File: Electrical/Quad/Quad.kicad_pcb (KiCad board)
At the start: 2 copper layers, 140 x 70 mm, 133 parts, among them J101 01x04, J102 01x04, J103 01x03, J104 01x03, J201 01x03, J202 01x04, J203 01x03, J204 01x04, J205 01x03, J206 USB_OTG, J207 01x04, J208 01x02, J209 01x04, J210 01x02, J211 01x02, J212 4PostTerm, J213 2PostTerm, J214 2PostTerm, J215 2PostTerm, J216 2PostTerm, J217 2PostTerm, J218 01x02, J219 01x02, Q201 FDC6420C, Q202 FDG1024NZ, Q301 FDC6420C, Q401 FDC6420C, Q501 FDC6420C, Q601 FDC6420C, U201 TPD4S012, U202 ACS723LLCTR-05AB-T, U203 ACS723LLCTR-05AB-T, U204 24LC256, U205 LM2576HVS-ADJ, U206 LM2576HVS-ADJ

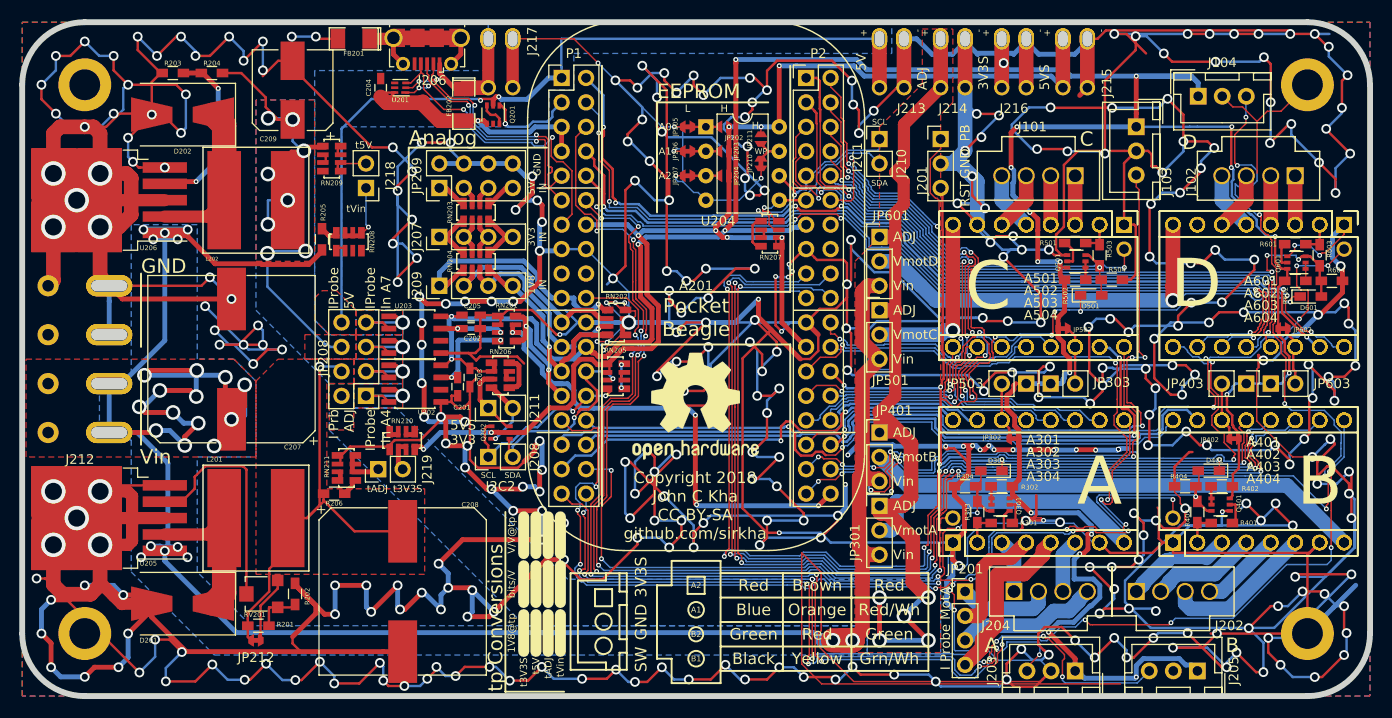
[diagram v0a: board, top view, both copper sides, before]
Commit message: Rearranged the power outputs to support TE Connectivity AMP connectors.
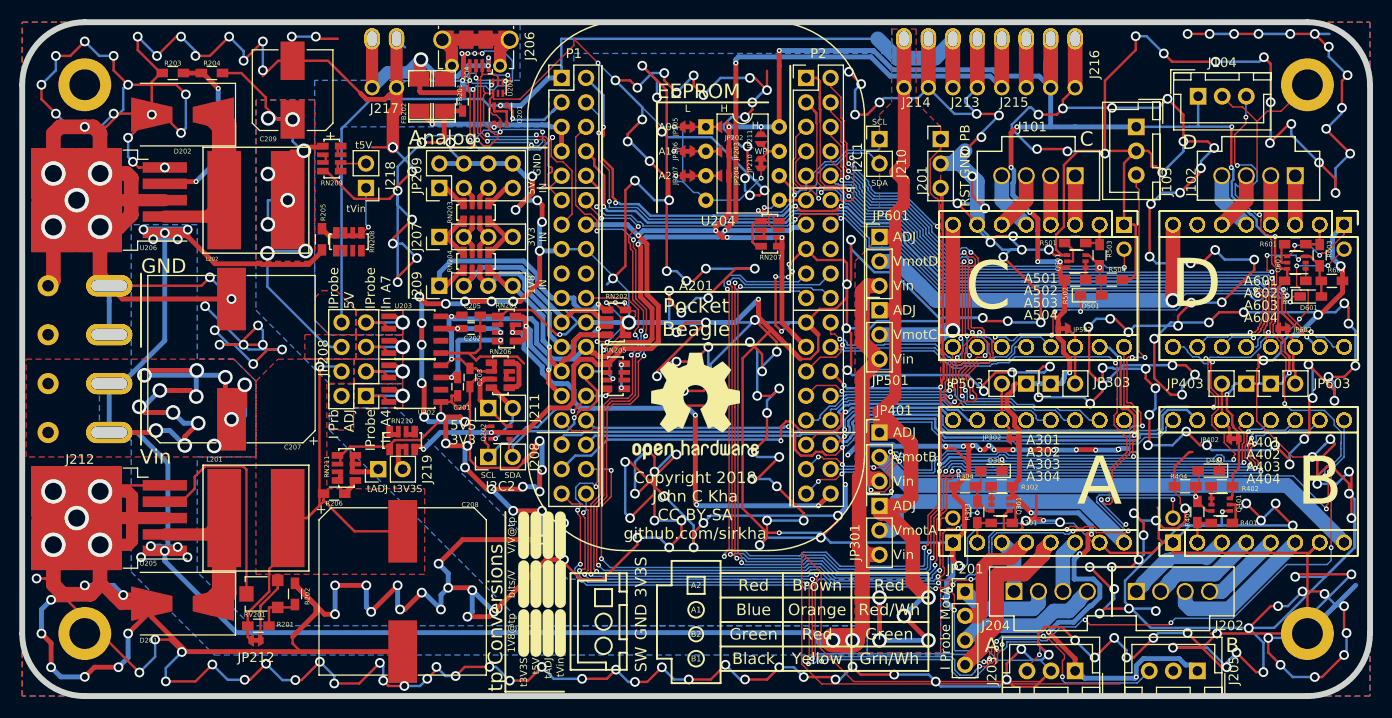
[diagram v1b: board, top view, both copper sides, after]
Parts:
- moved J217 12.1 mm to (67.6, 69.3)
- moved FB201 11.1 mm to (73.8, 72.6), turned to 90 degrees
- moved U201 10.2 mm to (79.4, 71.8), turned to 270 degrees
- moved C204 8.63 mm to (75.7, 73.3), turned to 270 degrees
- moved J213 7.62 mm to (127.9, 69.3)
- moved J215 6.35 mm to (133.0, 69.3)
- moved J206 5.08 mm to (77.1, 67.2)
- moved J216 5.08 mm to (138.1, 69.3)
- moved FB202 4.68 mm to (71.3, 72.6), turned to 90 degrees
- moved J214 3.81 mm to (122.9, 69.3)
- moved Q201 0.76 mm to (79.7, 74.6)
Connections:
- C204 pad 1: /Common/usb1_vbus -> /Common/usb1_5V
- FB201 pad 1: Net-(FB201-Pad1) -> GND
- FB201 pad 2: GND -> Net-(FB201-Pad2)
- FB202 pad 1: /Common/usb1_5V -> /Common/usb1_vbus
- FB202 pad 2: /Common/usb1_vbus -> /Common/usb1_5V
- J206 pad 6: Net-(FB201-Pad1) -> Net-(FB201-Pad2)
- U201 pad 6: /Common/usb1_vbus -> /Common/usb1_5V
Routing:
- net GND: track 2509.9 -> 2550.2 mm, vias 393 -> 404
- net 3V3S: track 353.1 -> 328.8 mm, vias 27 -> 25
- net Net-(FB201-Pad1): track 22.1 -> 0.00 mm
- net /Common/usb1_5V: track 11.8 -> 33.4 mm, vias 0 -> 4
- net Net-(FB201-Pad2): track 0.00 -> 15.0 mm
- net +5V: track 89.0 -> 97.5 mm, vias 2 -> 1
- net /Common/usb1_vbus: track 27.3 -> 18.9 mm, vias 1 -> 2
- net Vadj: track 98.5 -> 91.7 mm
- net 5VS: track 126.8 -> 120.7 mm
- net /Common/usb1_d-: track 29.0 -> 23.8 mm, vias 4 -> 2
- net (no net): track 0.00 -> 4.88 mm, vias 0 -> 2
- net /Common/usb1_d+: track 28.0 -> 25.3 mm
- net /Common/usb1_drvvbus: track 9.68 -> 10.2 mm, vias 2 -> 1
- net /Common/usb1_id: track 32.6 -> 32.7 mm, vias 2 -> 5
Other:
- outline, holes or cut-outs redrawn

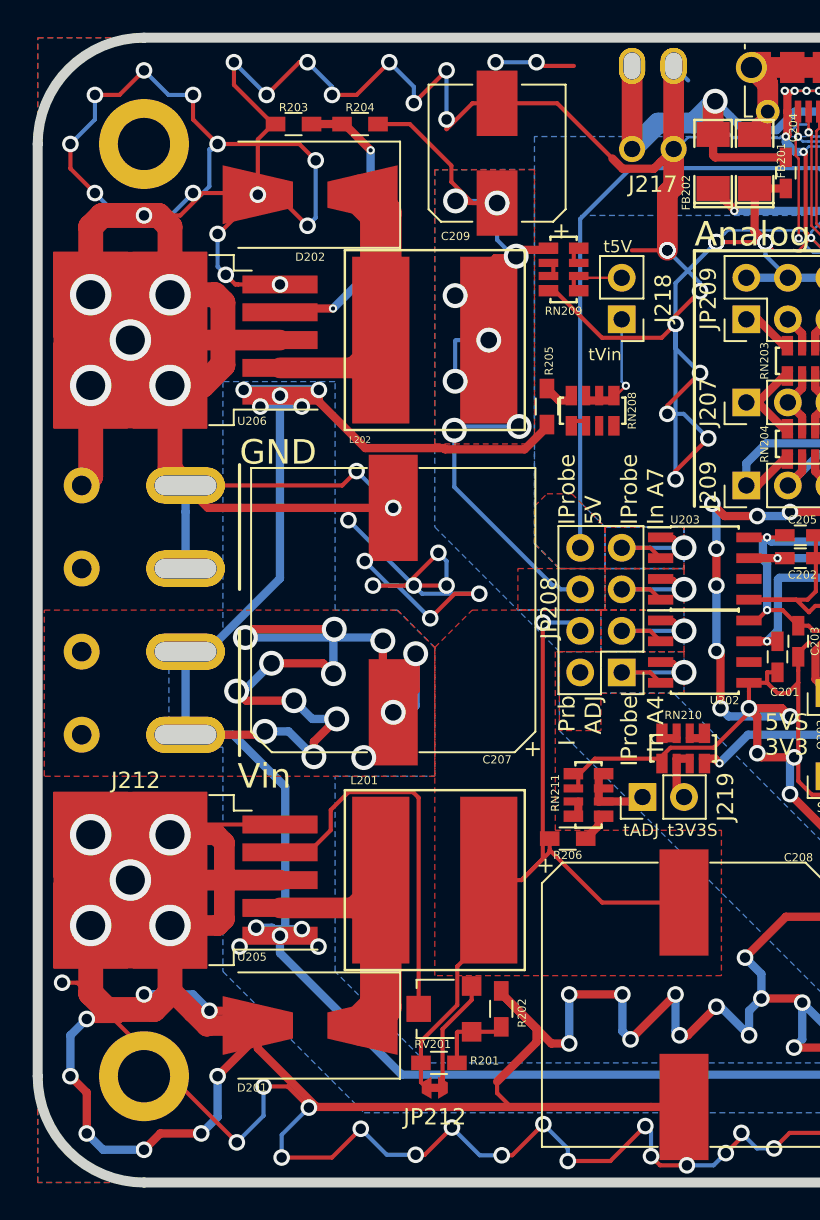
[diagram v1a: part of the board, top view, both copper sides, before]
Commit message: Modified main power input footprint to support other connectors
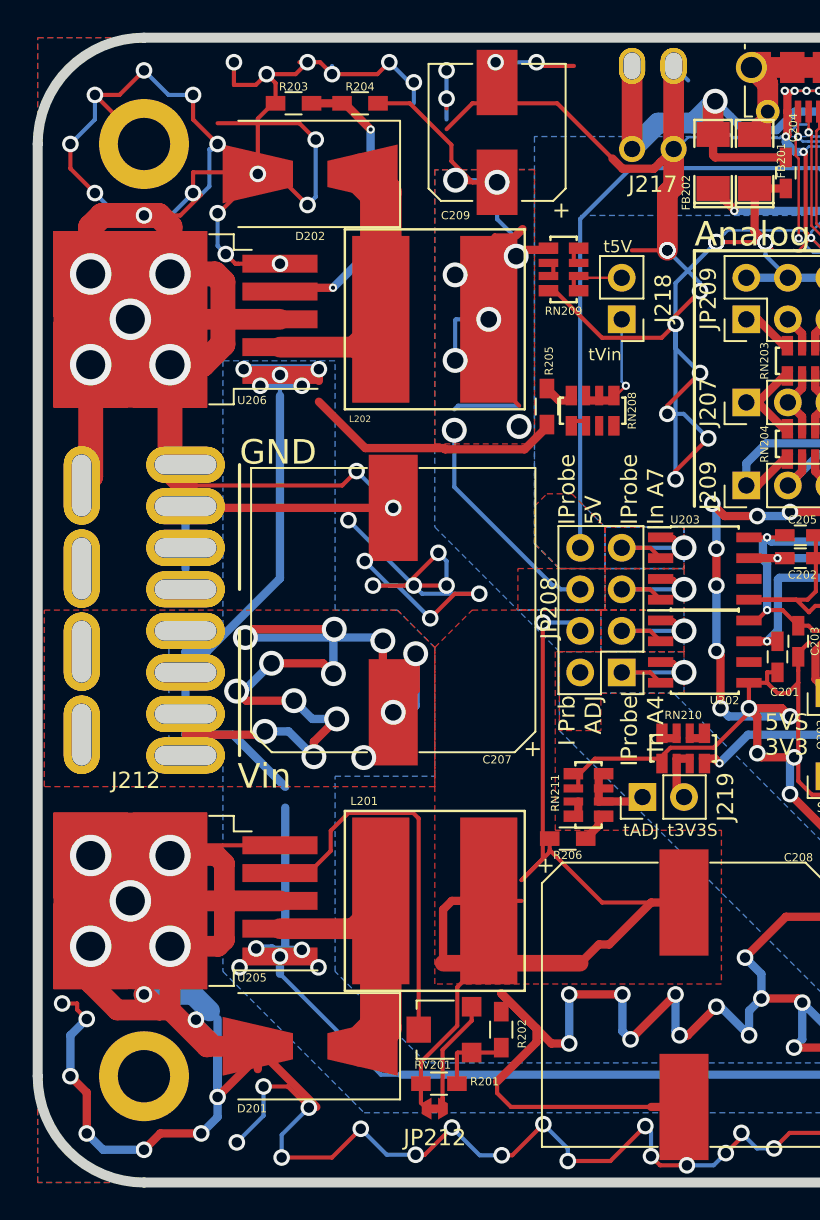
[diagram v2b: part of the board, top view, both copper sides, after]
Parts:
- moved C209 1.27 mm to (58.1, 70.8)
- moved D201 1.27 mm to (46.7, 126.7)
- moved D202 1.27 mm to (46.7, 73.3)
- moved L201 1.27 mm to (54.3, 117.8)
- moved L202 1.27 mm to (54.3, 82.2)
- moved R202 1.27 mm to (58.3, 125.7)
- moved R203 1.27 mm to (45.6, 69.0)
- moved R204 1.27 mm to (49.7, 69.0)
- moved RV201 1.27 mm to (54.9, 125.7)
- moved U205 1.27 mm to (39.0, 117.8)
- moved U206 1.27 mm to (39.0, 82.2)
- moved JP212 1.27 mm to (54.3, 130.5)
- moved R201 1.27 mm to (54.5, 129.0)
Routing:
- net GND: track 2550.2 -> 2514.6 mm
- net /Common/IP_vadj: track 48.1 -> 70.7 mm
- net /Common/IP_5V: track 57.0 -> 53.0 mm, vias 8 -> 7
- net (no net): track 4.88 -> 7.65 mm, vias 2 -> 3
- net Vin: track 273.4 -> 274.0 mm
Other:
- outline, holes or cut-outs redrawn

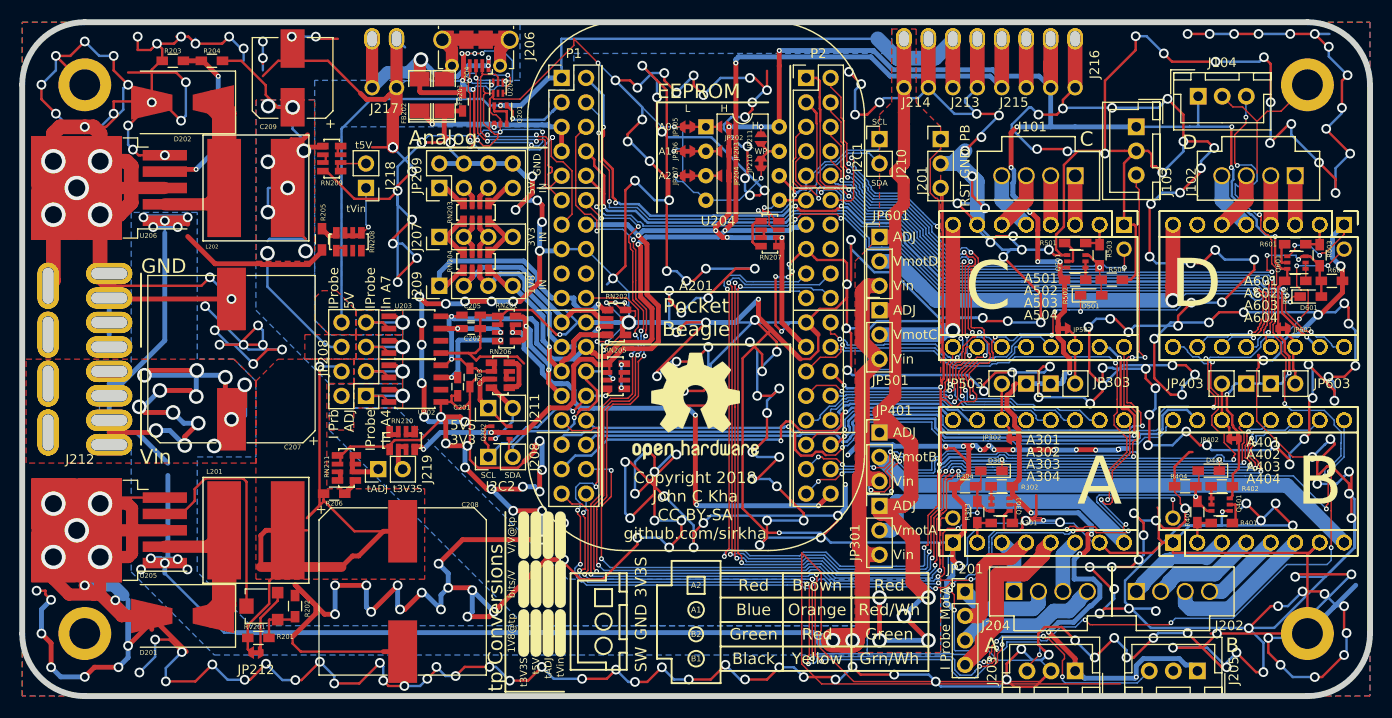
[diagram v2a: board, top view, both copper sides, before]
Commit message: Rearranged EEPROM to add an MSOP option and make the address/WP pins more accessible
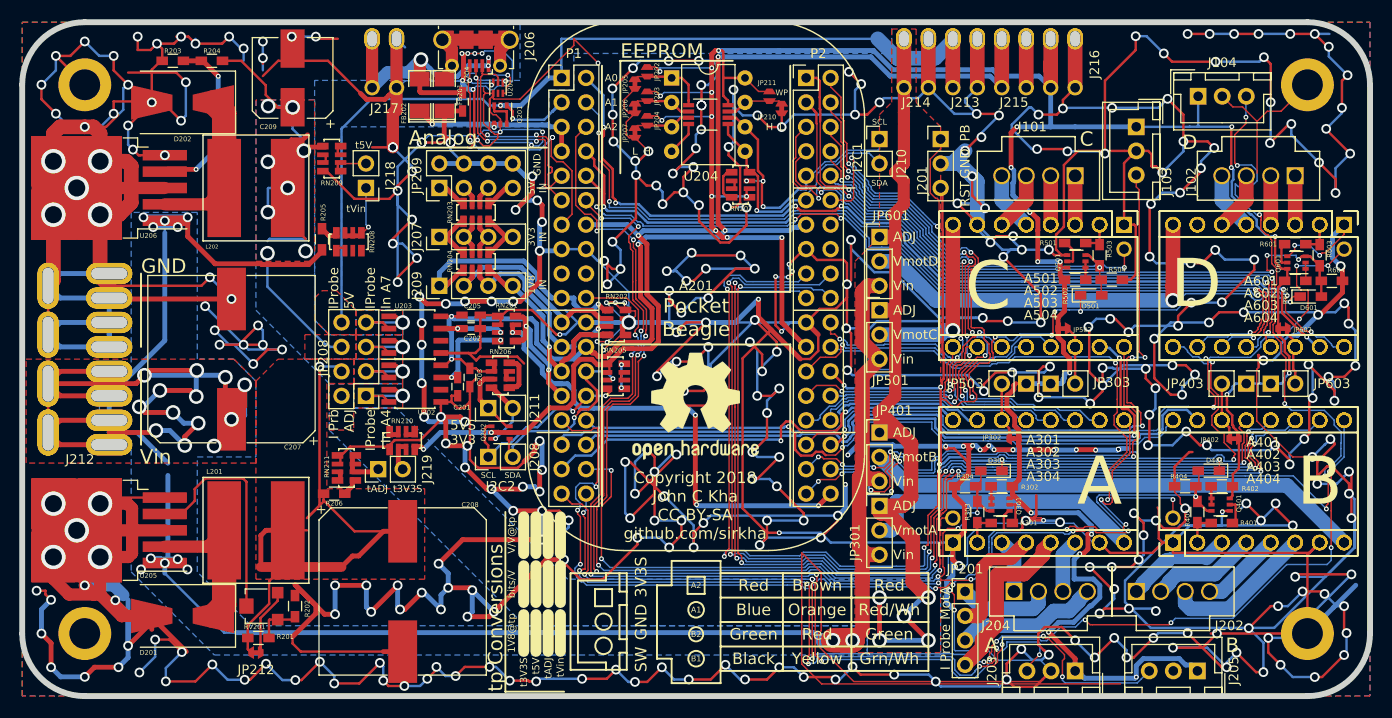
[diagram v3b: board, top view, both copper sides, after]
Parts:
- U204: footprint Housings_DIP:DIP-8_W7.62mm -> footprints:Dip-MSOP-8
- moved JP202 9.83 mm to (94.9, 70.2), turned to 270 degrees
- moved JP203 9.83 mm to (94.9, 72.7), turned to 270 degrees
- moved JP204 9.83 mm to (94.9, 75.2), turned to 270 degrees
- moved JP205 7.04 mm to (93.7, 71.4), turned to 90 degrees
- moved JP207 7.04 mm to (93.7, 76.5), turned to 90 degrees
- moved JP206 7.04 mm to (93.7, 74.0), turned to 90 degrees
- moved U204 6.20 mm to (97.5, 70.8)
- moved JP210 6.11 mm to (108.9, 74.0)
- moved RN207 5.92 mm to (104.6, 81.9)
- moved JP211 4.53 mm to (107.6, 72.7)
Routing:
- net Vin: track 274.0 -> 322.8 mm
- net 3V3S: track 328.8 -> 365.9 mm, vias 25 -> 31
- net GND: track 2514.6 -> 2547.0 mm, vias 404 -> 409
- net /Common/i2c1_sda: track 18.3 -> 27.5 mm
- net /Common/i2c1_scl: track 23.3 -> 29.6 mm, vias 2 -> 3
- net Net-(JP202-Pad2): track 2.81 -> 8.16 mm
- net Net-(JP203-Pad2): track 2.81 -> 6.13 mm
- net Net-(JP204-Pad2): track 2.81 -> 6.13 mm
- net Net-(JP210-Pad2): track 3.31 -> 6.13 mm
- net 5VS: track 120.7 -> 122.5 mm
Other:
- net class Default: clearance 0.152146 -> 0.14986
- net class Minimum: clearance 0.152146 -> 0.14986
- rule trace_clearance: 0.152146 -> 0.14986
- rule trace_min: 0.152375 -> 0.1524

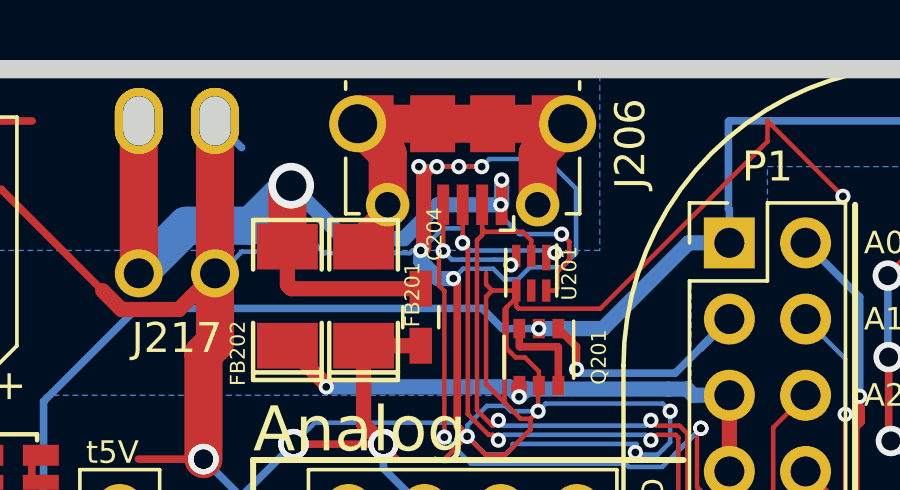
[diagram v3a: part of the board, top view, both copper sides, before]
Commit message: Fixed footprint (kicad library is wrong?)
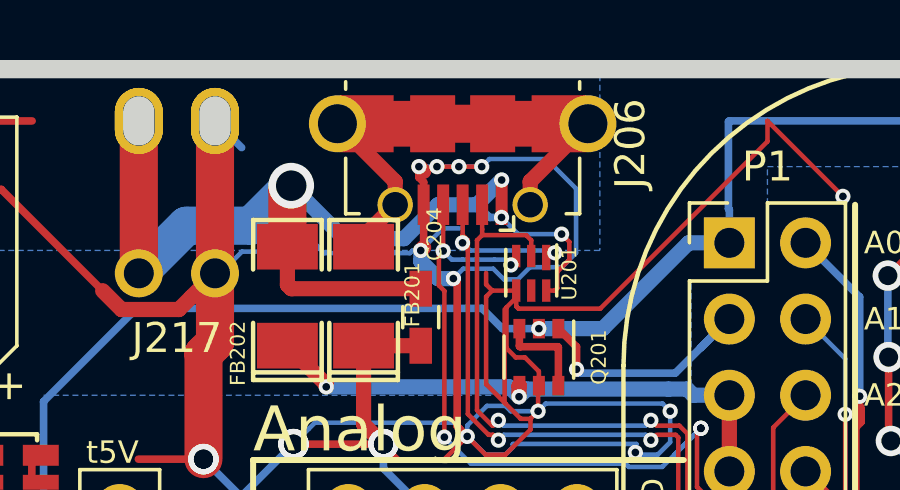
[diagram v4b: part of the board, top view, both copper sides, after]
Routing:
- net Net-(FB201-Pad2): track 15.0 -> 17.2 mm
- net /Common/usb1_5V: track 33.4 -> 34.7 mm
- net GND: track 2547.0 -> 2545.8 mm
